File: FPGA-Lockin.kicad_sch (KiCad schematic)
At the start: 25 parts, among them J6 Conn_02x07_Odd_Even, J7 Conn_01x02_Pin, U1 ICE40UP5K-SG48ITR, U7 STM32F405RGTx

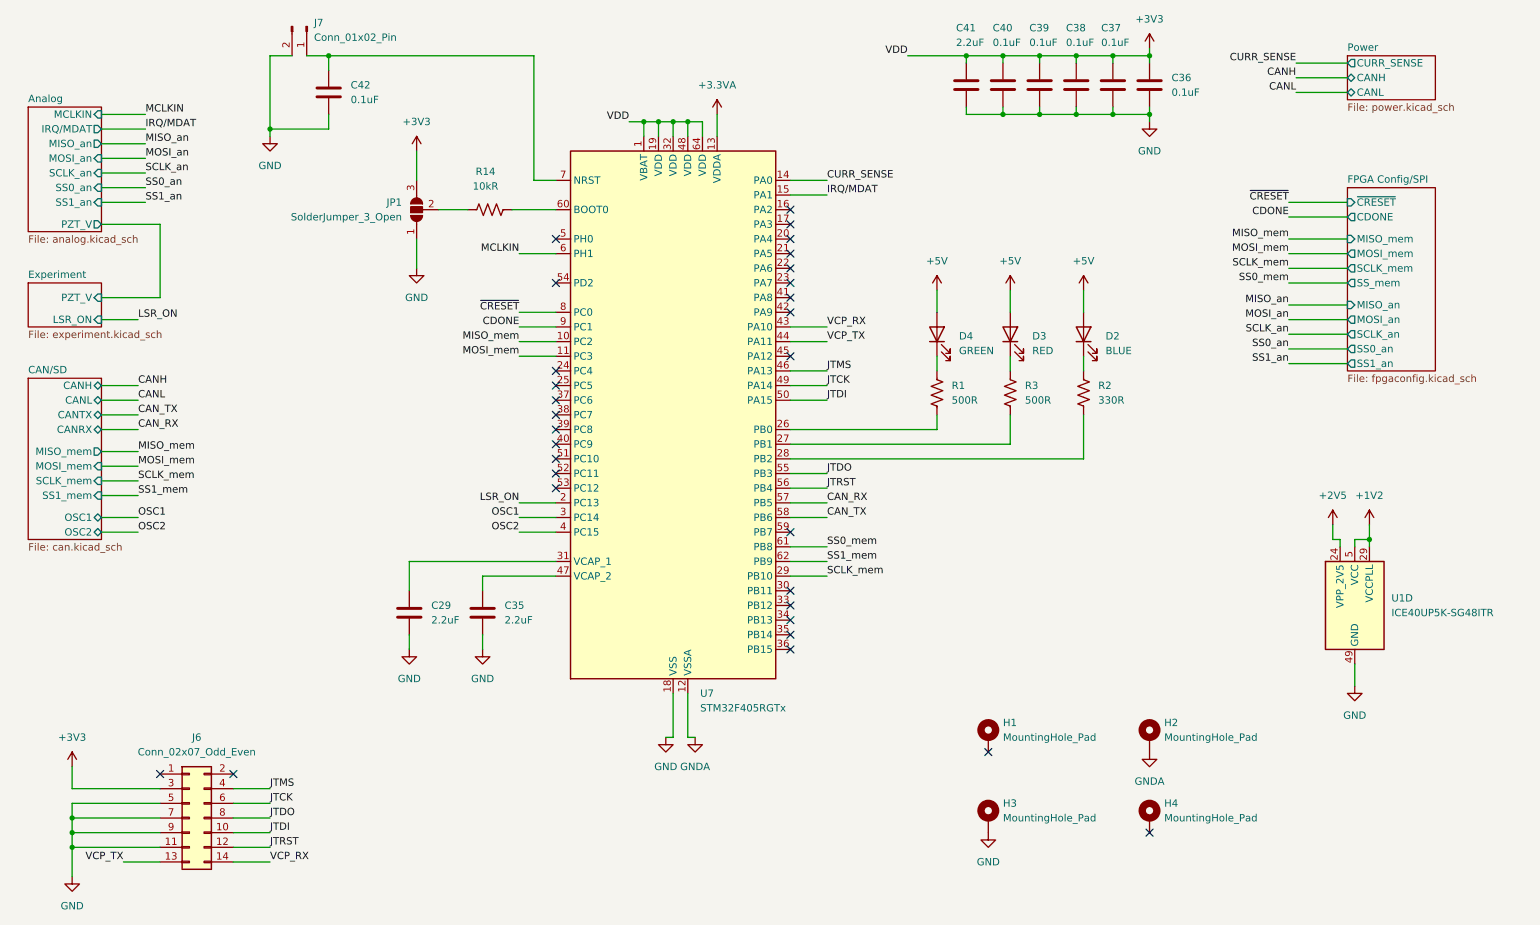
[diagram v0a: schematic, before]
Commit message: Fix review suggestions from non-fpga board
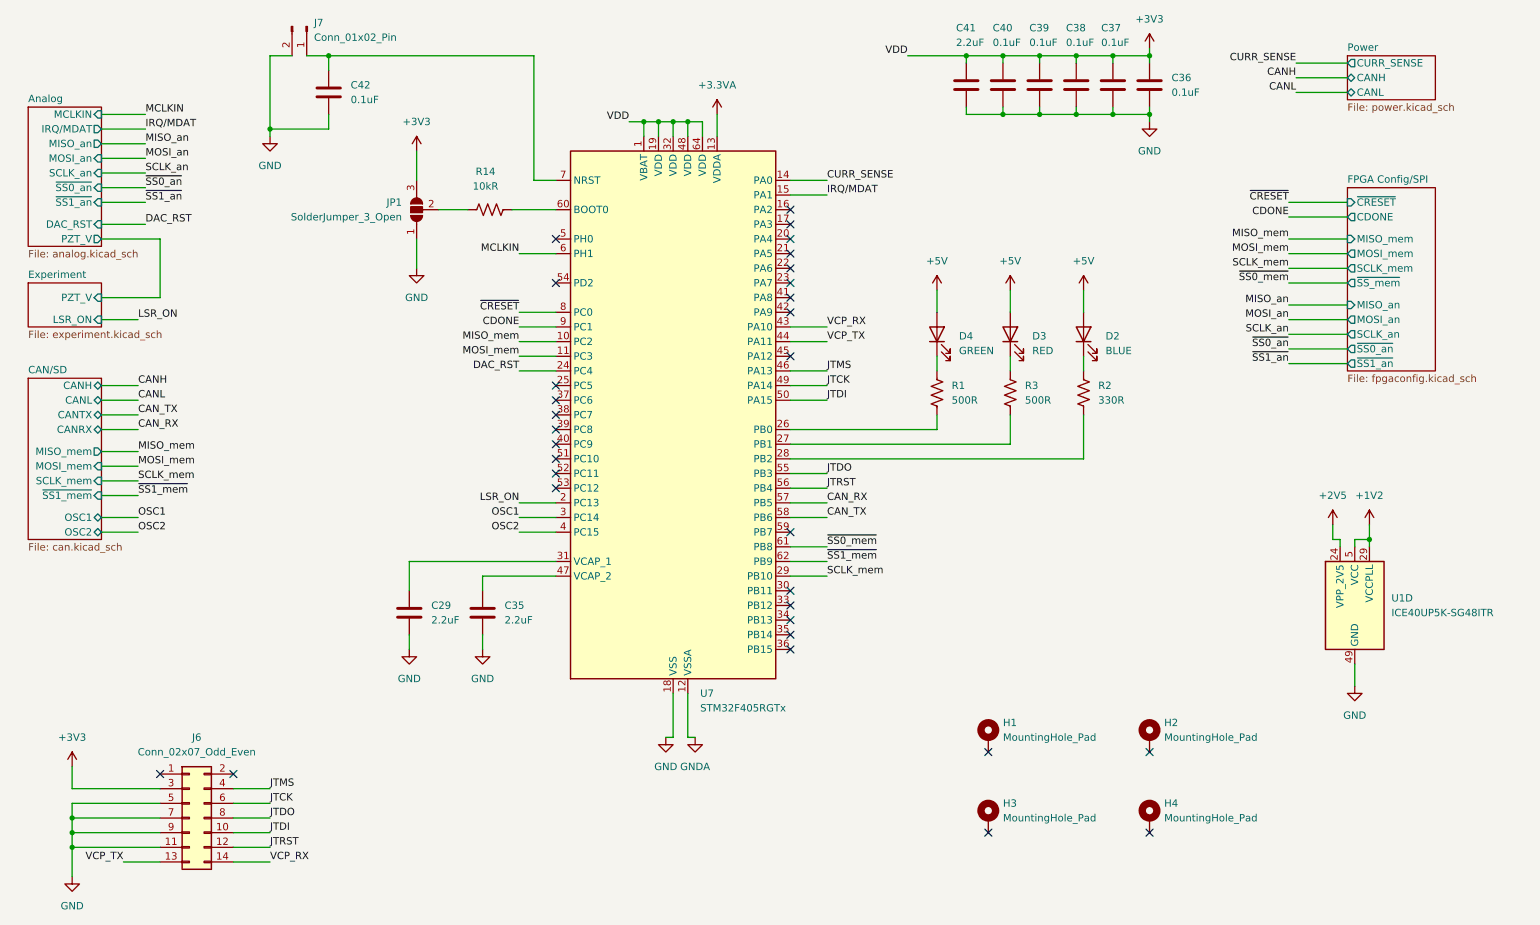
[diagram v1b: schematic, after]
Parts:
- D2, D3, D4: footprint LED_SMD:LED_0805_2012Metric_Pad1.15x1.40mm_HandSolder -> LED_SMD:LED_1206_3216Metric_Pad1.42x1.75mm_HandSolder
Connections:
- net GND: no longer H3.1
- net GNDA: no longer H2.1
- net DAC_RST: now reaches U7.24 (PC4)
- net SS0_mem renamed ~{SS0_mem}
- net SS1_mem renamed ~{SS1_mem}
- no-connect marks 30 -> 31
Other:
- sheet Analog ports: added DAC_RST, ~{SS0_an}, ~{SS1_an}; removed SS0_an, SS1_an
- sheet CAN/SD ports: added ~{SS1_mem}; removed SS1_mem
- sheet FPGA Config/SPI ports: added ~{SS0_an}, ~{SS1_an}, ~{SS_mem}; removed SS0_an, SS1_an, SS_mem
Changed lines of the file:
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@@
 	)
 	(no_connect
-		(at 115.57 77.47)
+		(at 190.5 157.48)
 	)
 	(no_connect
@@
 	)
 	(no_connect
+		(at 218.44 143.51)
+	)
+	(no_connect
 		(at 156.21 62.23)
 	)
@@
 	(wire
 		(pts
+			(xy 36.83 52.07) (xy 44.45 52.07)
+		)
+		(stroke
+			(width 0)
+			(type default)
+		)
+	)
+	(wire
+		(pts
 			(xy 36.83 33.02) (xy 44.45 33.02)
 		)
@@
 	(wire
 		(pts
-			(xy 46.99 64.77) (xy 46.99 52.07)
+			(xy 46.99 64.77) (xy 46.99 54.61)
 		)
 		(stroke
@@
 	(wire
 		(pts
-			(xy 46.99 52.07) (xy 36.83 52.07)
+			(xy 46.99 54.61) (xy 36.83 54.61)
 		)
 		(stroke
@@
 	(wire
 		(pts
+			(xy 109.22 77.47) (xy 115.57 77.47)
+		)
+		(stroke
+			(width 0)
+			(type default)
+		)
+	)
+	(wire
+		(pts
 			(xy 31.75 149.86) (xy 31.75 146.05)
 		)
@@
 		)
 	)
-	(label "SS1_mem"
+	(label "~{SS1_mem}"
 		(at 43.18 99.06 0)
 		(effects
@@
 		)
 	)
-	(label "SS1_an"
+	(label "~{SS1_an}"
 		(at 44.45 48.26 0)
 		(effects
@@
 		)
 	)
-	(label "SS0_mem"
+	(label "~{SS0_mem}"
 		(at 162.56 107.95 0)
 		(effects
@@
 		)
 	)
-	(label "SS0_an"
+	(label "DAC_RST"
+		(at 109.22 77.47 180)
+		(effects
+			(font
+				(size 1.27 1.27)
+			)
+			(justify right bottom)
+		)
+	)
+	(label "~{SS0_an}"
 		(at 44.45 45.72 0)
 		(effects
@@
 		)
 	)
-	(label "SS1_an"
+	(label "~{SS1_an}"
 		(at 242.57 76.2 180)
 		(effects
@@
 		)
 	)
+	(label "DAC_RST"
+		(at 44.45 52.07 0)
+		(effects
+			(font
+				(size 1.27 1.27)
+			)
+			(justify left bottom)
+		)
+	)
 	(label "MISO_mem"
 		(at 109.22 72.39 180)
@@
 		)
 	)
-	(label "SS0_mem"
+	(label "~{SS0_mem}"
 		(at 242.57 62.23 180)
 		(effects
@@
 		)
 	)
-	(label "SS1_mem"
+	(label "~{SS1_mem}"
 		(at 162.56 110.49 0)
 		(effects
@@
 		)
 	)
-	(label "SS0_an"
+	(label "~{SS0_an}"
 		(at 242.57 73.66 180)
 		(effects
@@
 			)
 		)
-		(property "Footprint" "LED_SMD:LED_0805_2012Metric_Pad1.15x1.40mm_HandSolder"
+		(property "Footprint" "LED_SMD:LED_1206_3216Metric_Pad1.42x1.75mm_HandSolder"
 			(at 207.01 71.12 0)
 			(effects
@@
 			)
 		)
-		(property "Footprint" "LED_SMD:LED_0805_2012Metric_Pad1.15x1.40mm_HandSolder"
+		(property "Footprint" "LED_SMD:LED_1206_3216Metric_Pad1.42x1.75mm_HandSolder"
 			(at 181.61 71.12 0)
 			(effects
@@
 			)
 		)
-		(property "Footprint" "LED_SMD:LED_0805_2012Metric_Pad1.15x1.40mm_HandSolder"
+		(property "Footprint" "LED_SMD:LED_1206_3216Metric_Pad1.42x1.75mm_HandSolder"
 			(at 194.31 71.12 0)
 			(effects
@@
 	)
 	(symbol
-		(lib_id "power:GNDA")
-		(at 218.44 143.51 0)
-		(unit 1)
-		(exclude_from_sim no)
-		(in_bom yes)
-		(on_board yes)
-		(dnp no)
-		(fields_autoplaced yes)
-		(property "Reference" "#PWR093"
-			(at 218.44 149.86 0)
-			(effects
-				(font
-					(size 1.27 1.27)
-				)
-				(hide yes)
-			)
-		)
-		(property "Value" "GNDA"
-			(at 218.44 148.59 0)
-			(effects
-				(font
-					(size 1.27 1.27)
-				)
-			)
-		)
-		(property "Footprint" ""
-			(at 218.44 143.51 0)
-			(effects
-				(font
-					(size 1.27 1.27)
-				)
-				(hide yes)
-			)
-		)
-		(property "Datasheet" ""
-			(at 218.44 143.51 0)
-			(effects
-				(font
-					(size 1.27 1.27)
-				)
-				(hide yes)
-			)
-		)
-		(property "Description" "Power symbol creates a global label with name \"GNDA\" , analog ground"
-			(at 218.44 143.51 0)
-			(effects
-				(font
-					(size 1.27 1.27)
-				)
-				(hide yes)
-			)
-		)
-		(pin "1"
-		)
-		(instances
-			(project ""
-				(path "/0d4da0fe-f3e4-47fc-a7f7-d58161fd7b20"
-					(reference "#PWR093")
-					(unit 1)
-				)
-			)
-		)
-	)
-	(symbol
-		(lib_id "power:GND")
-		(at 190.5 157.48 0)
-		(unit 1)
-		(exclude_from_sim no)
-		(in_bom yes)
-		(on_board yes)
-		(dnp no)
-		(fields_autoplaced yes)
-		(property "Reference" "#PWR092"
-			(at 190.5 163.83 0)
-			(effects
-				(font
-					(size 1.27 1.27)
-				)
-				(hide yes)
-			)
-		)
-		(property "Value" "GND"
-			(at 190.5 162.56 0)
-			(effects
-				(font
-					(size 1.27 1.27)
-				)
-			)
-		)
-		(property "Footprint" ""
-			(at 190.5 157.48 0)
-			(effects
-				(font
-					(size 1.27 1.27)
-				)
-				(hide yes)
-			)
-		)
-		(property "Datasheet" ""
-			(at 190.5 157.48 0)
-			(effects
-				(font
-					(size 1.27 1.27)
-				)
-				(hide yes)
-			)
-		)
-		(property "Description" "Power symbol creates a global label with name \"GND\" , ground"
-			(at 190.5 157.48 0)
-			(effects
-				(font
-					(size 1.27 1.27)
-				)
-				(hide yes)
-			)
-		)
-		(pin "1"
-		)
-		(instances
-			(project ""
-				(path "/0d4da0fe-f3e4-47fc-a7f7-d58161fd7b20"
-					(reference "#PWR092")
-					(unit 1)
-				)
-			)
-		)
-	)
-	(symbol
 		(lib_id "Device:C")
 		(at 193.04 27.94 0)
@@
 	(sheet
 		(at 24.13 31.75)
-		(size 12.7 21.59)
+		(size 12.7 24.13)
 		(exclude_from_sim no)
 		(in_bom yes)
@@
 		)
 		(property "Sheetfile" "analog.kicad_sch"
-			(at 24.13 53.9246 0)
+			(at 24.13 56.4646 0)
 			(effects
 				(font
@@
 		)
 		(pin "PZT_V" output
-			(at 36.83 52.07 0)
+			(at 36.83 54.61 0)
 			(effects
 				(font
@@
 			)
 		)
-		(pin "SS1_an" input
-			(at 36.83 48.26 0)
+		(pin "MOSI_an" input
+			(at 36.83 40.64 0)
 			(effects
 				(font
@@
 			)
 		)
-		(pin "MOSI_an" input
-			(at 36.83 40.64 0)
+		(pin "MISO_an" output
+			(at 36.83 38.1 0)
 			(effects
 				(font
@@
 			)
 		)
-		(pin "MISO_an" output
-			(at 36.83 38.1 0)
+		(pin "MCLKIN" input
+			(at 36.83 33.02 0)
 			(effects
 				(font
@@
 			)
 		)
-		(pin "SS0_an" input
+		(pin "~{SS1_an}" input
+			(at 36.83 48.26 0)
+			(effects
+				(font
+					(size 1.27 1.27)
+				)
+				(justify right)
+			)
+		)
+		(pin "~{SS0_an}" input
 			(at 36.83 45.72 0)
 			(effects
@@
 			)
 		)
-		(pin "MCLKIN" input
-			(at 36.83 33.02 0)
+		(pin "DAC_RST" input
+			(at 36.83 52.07 0)
 			(effects
 				(font
@@
 			)
 		)
-		(pin "SS_mem" output
-			(at 252.73 62.23 180)
-			(effects
-				(font
-					(size 1.27 1.27)
-				)
-				(justify left)
-			)
-		)
 		(pin "MOSI_mem" output
 			(at 252.73 57.15 180)
@@
 			)
 		)
-		(pin "SS1_an" output
-			(at 252.73 76.2 180)
+		(pin "MISO_an" input
+			(at 252.73 66.04 180)
 			(effects
 				(font
@@
 			)
 		)
-		(pin "SS0_an" output
-			(at 252.73 73.66 180)
+		(pin "SCLK_mem" output
+			(at 252.73 59.69 180)
 			(effects
 				(font
@@
 			)
 		)
-		(pin "MISO_an" input
-			(at 252.73 66.04 180)
+		(pin "SCLK_an" output
+			(at 252.73 71.12 180)
 			(effects
 				(font
@@
 			)
 		)
-		(pin "SCLK_mem" output
-			(at 252.73 59.69 180)
+		(pin "~{SS_mem}" output
+			(at 252.73 62.23 180)
 			(effects
 				(font
@@
 			)
 		)
-		(pin "SCLK_an" output
-			(at 252.73 71.12 180)
+		(pin "~{SS0_an}" output
+			(at 252.73 73.66 180)
+			(effects
+				(font
+					(size 1.27 1.27)
+				)
+				(justify left)
+			)
+		)
+		(pin "~{SS1_an}" output
+			(at 252.73 76.2 180)
 			(effects
 				(font
@@
 			)
 		)
-		(pin "SS1_mem" input
-			(at 36.83 99.06 0)
-			(effects
-				(font
-					(size 1.27 1.27)
-				)
-				(justify right)
-			)
-		)
 		(pin "SCLK_mem" input
 			(at 36.83 96.52 0)
@@
 			(effects
 				(font
+					(size 1.27 1.27)
+				)
+				(justify right)
+			)
+		)
+		(pin "~{SS1_mem}" input
+			(at 36.83 99.06 0)
+			(effects
+				(font

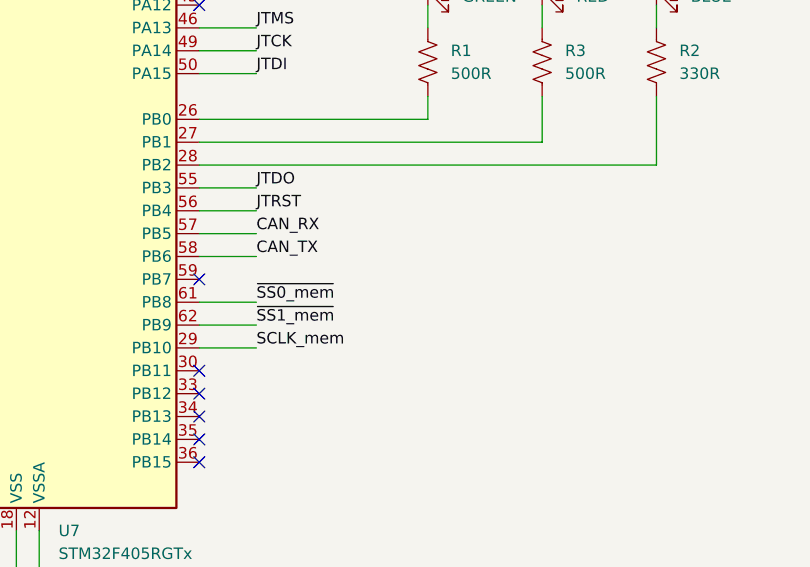
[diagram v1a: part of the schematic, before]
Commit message: Fix diode
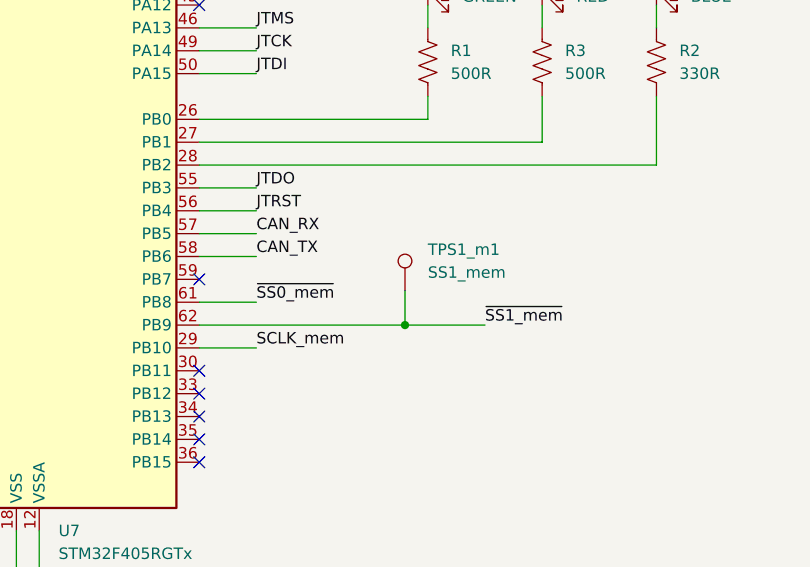
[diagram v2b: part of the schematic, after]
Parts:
- added TPS1_m1: SS1_mem, TestPoint:TestPoint_Pad_D1.0mm, symbol Connector:TestPoint
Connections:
- net ~{SS1_mem}: now also TPS1_m1.1
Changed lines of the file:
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@@
+	)
+	(junction
+		(at 179.07 110.49)
+		(diameter 0)
+		(color 0 0 0 0)
 	)
 	(junction
@@
 	(wire
 		(pts
+			(xy 179.07 106.68) (xy 179.07 110.49)
+		)
+		(stroke
+			(width 0)
+			(type default)
+		)
+	)
+	(wire
+		(pts
 			(xy 156.21 72.39) (xy 162.56 72.39)
 		)
@@
 	(wire
 		(pts
+			(xy 179.07 110.49) (xy 187.96 110.49)
+		)
+		(stroke
+			(width 0)
+			(type default)
+		)
+	)
+	(wire
+		(pts
 			(xy 90.17 110.49) (xy 90.17 115.57)
 		)
@@
 	(wire
 		(pts
-			(xy 156.21 110.49) (xy 162.56 110.49)
+			(xy 156.21 110.49) (xy 179.07 110.49)
 		)
 		(stroke
@@
 	)
 	(label "~{SS1_mem}"
-		(at 162.56 110.49 0)
+		(at 187.96 110.49 0)
 		(effects
 			(font
@@
 					(unit 1)
 				)
+			)
+		)
+	)
+	(symbol
+		(lib_id "Connector:TestPoint")
+		(at 179.07 106.68 0)
+		(unit 1)
+		(exclude_from_sim no)
+		(in_bom yes)
+		(on_board yes)
+		(dnp no)
+		(fields_autoplaced yes)
+		(property "Reference" "TPS1_m1"
+			(at 181.61 102.1079 0)
+			(effects
+				(font
+					(size 1.27 1.27)
+				)
+				(justify left)
+			)
+		)
+		(property "Value" "SS1_mem"
+			(at 181.61 104.6479 0)
+			(effects
+				(font
+					(size 1.27 1.27)
+				)
+				(justify left)
+			)
+		)
+		(property "Footprint" "TestPoint:TestPoint_Pad_D1.0mm"
+			(at 184.15 106.68 0)
+			(effects
+				(font
+					(size 1.27 1.27)
+				)
+				(hide yes)
+			)
+		)
+		(property "Datasheet" "~"
+			(at 184.15 106.68 0)
+			(effects
+				(font
+					(size 1.27 1.27)
+				)
+				(hide yes)
+			)
+		)
+		(property "Description" "test point"
+			(at 179.07 106.68 0)
+			(effects
+				(font
+					(size 1.27 1.27)
+				)
+				(hide yes)
+			)
+		)
+		(pin "1"
+		)
+		(instances
+			(project ""
+				(path "/0d4da0fe-f3e4-47fc-a7f7-d58161fd7b20"
+					(reference "TPS1_m1")
+					(unit 1)
+				)
